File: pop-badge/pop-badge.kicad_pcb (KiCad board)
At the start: 2 copper layers, 155.4 x 107.4 mm, 148 parts, among them J1 Conn_01x04, Q1 BC818, U1 WS2812-2020, U10 WS2812-2020, U11 WS2812-2020, U12 WS2812-2020, U13 WS2812-2020, U14 WS2812-2020, U15 WS2812-2020, U16 WS2812-2020, U17 WS2812-2020, U18 WS2812-2020, U19 WS2812-2020, U2 WS2812-2020, U20 WS2812-2020, U21 WS2812-2020, U22 WS2812-2020, U23 WS2812-2020, U24 WS2812-2020, U25 WS2812-2020, U3 WS2812-2020, U4 WS2812-2020, U5 WS2812-2020, U6 WS2812-2020, U7 WS2812-2020, U8 WS2812-2020, U9 WS2812-2020

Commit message: much more layouting
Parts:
- removed D51, D52, D53, D54, D55, D56, D57, D58, D59, D60: LED, LED_SMD:LED_0603_1608Metric
- removed the R51 at (158.2, 69.0)
- removed R52, R53, R54, R55, R56, R57, R58, R59, R60: 100, Resistor_SMD:R_0603_1608Metric_Pad1.05x0.95mm_HandSolder
- added H1: MountingHole, MountingHole:MountingHole_4.3mm_M4, F.Cu at (48.3, 72.4)
- added H2: MountingHole, MountingHole:MountingHole_4.3mm_M4, F.Cu at (95.2, 72.4)
- J1: moved to B.Cu
- moved R18 122.2 mm to (74.3, 131.6), turned to 270 degrees
- moved R12 109.0 mm to (102.1, 87.2), turned to 90 degrees
- moved R22 107.0 mm to (70.4, 125.1), turned to 270 degrees
- moved R41 106.2 mm to (78.9, 123.8), turned to 270 degrees
- moved R30 102.9 mm to (66.5, 118.0), turned to 270 degrees
- moved R2 102.8 mm to (50.7, 121.7), turned to 270 degrees
- moved D27 102.1 mm to (58.7, 49.4)
- moved R16 100.7 mm to (82.5, 72.8), turned to 90 degrees
- moved R29 98.3 mm to (35.3, 128.9), turned to 180 degrees
- moved R5 97.5 mm to (30.9, 123.7), turned to 180 degrees
- moved R25 95.1 mm to (41.1, 123.3), turned to 270 degrees
- moved R39 94.6 mm to (109.3, 124.5), turned to 270 degrees
- moved R21 91.9 mm to (25.3, 131.1), turned to 180 degrees
- moved R43 90.1 mm to (87.5, 115.2), turned to 270 degrees
- moved D3 88.3 mm to (64.8, 54.0), turned to 180 degrees
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- renumbered R61 to R51
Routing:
- net LEDw+: track 71.9 -> 247.1 mm
- net Net-(U10-Pad1): track 0.00 -> 15.1 mm
- net Net-(U21-Pad1): track 0.00 -> 13.8 mm
- net Net-(U18-Pad1): track 0.00 -> 13.4 mm
- net Net-(U17-Pad1): track 0.00 -> 12.6 mm
- net Net-(U12-Pad1): track 0.00 -> 12.2 mm
- net Net-(U5-Pad1): track 0.00 -> 11.0 mm
- net Net-(U11-Pad1): track 0.00 -> 10.2 mm
- net Net-(U24-Pad1): track 0.00 -> 9.82 mm
- net Net-(U7-Pad1): track 0.00 -> 8.84 mm
- net Net-(U6-Pad1): track 0.00 -> 6.83 mm
- net Net-(U4-Pad1): track 0.00 -> 6.48 mm
- net Net-(U3-Pad1): track 0.00 -> 6.36 mm
- net Net-(U2-Pad1): track 0.00 -> 6.36 mm
- net Net-(U1-Pad1): track 0.00 -> 6.36 mm
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- removed copper zone on B.Cu, net LEDw-
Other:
- board size 155.4 x 107.4 mm -> 129.5 x 101.3 mm

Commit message: routing mostly done
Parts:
- moved R21 3.25 mm to (23.2, 128.5)
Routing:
- net LEDw+: track 247.1 -> 619.3 mm
- net Net-(D20-Pad2): track 0.00 -> 4.20 mm
- net Net-(D14-Pad2): track 0.00 -> 3.43 mm
- net Net-(D12-Pad2): track 0.00 -> 2.95 mm
- net Net-(D36-Pad2): track 0.00 -> 2.95 mm
- net Net-(D23-Pad2): track 0.00 -> 2.88 mm
- net Net-(D31-Pad2): track 0.00 -> 2.82 mm
- net Net-(D27-Pad2): track 0.00 -> 2.82 mm
- net Net-(D3-Pad2): track 0.00 -> 2.82 mm
- net Net-(D42-Pad2): track 0.00 -> 2.78 mm
- net Net-(D11-Pad2): track 0.00 -> 2.72 mm
- net Net-(D47-Pad2): track 0.00 -> 2.69 mm
- net Net-(D33-Pad2): track 0.00 -> 2.66 mm
- net Net-(D38-Pad2): track 0.00 -> 2.53 mm
- net Net-(D45-Pad2): track 0.00 -> 2.52 mm
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
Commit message: current state
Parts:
- moved J1 38.7 mm to (56.9, 108.8), turned to 0 degrees
- moved Q1 33.9 mm to (63.9, 105.7)
- moved R51 32.6 mm to (60.6, 105.0), turned to 180 degrees
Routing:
- net LEDw-: track 3.82 -> 39.8 mm, vias 3 -> 16
- net LEDw+: track 619.3 -> 640.3 mm
- net /RGB LEDs/DIN: track 0.00 -> 14.5 mm, vias 0 -> 2
- net GND: track 0.00 -> 6.39 mm
- added copper zone on B.Cu, net LEDw-

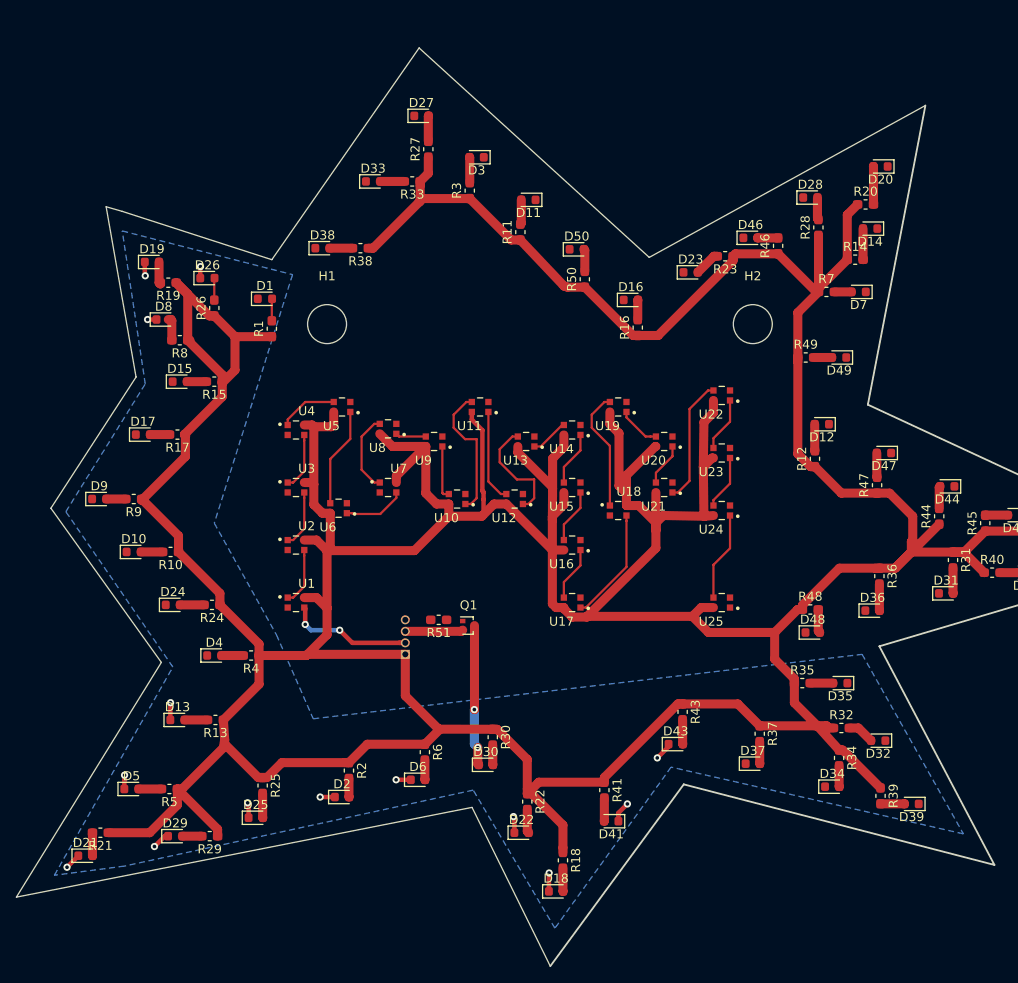
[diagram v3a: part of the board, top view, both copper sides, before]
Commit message: import decoupling caps and remove power lines for redo for ws2812
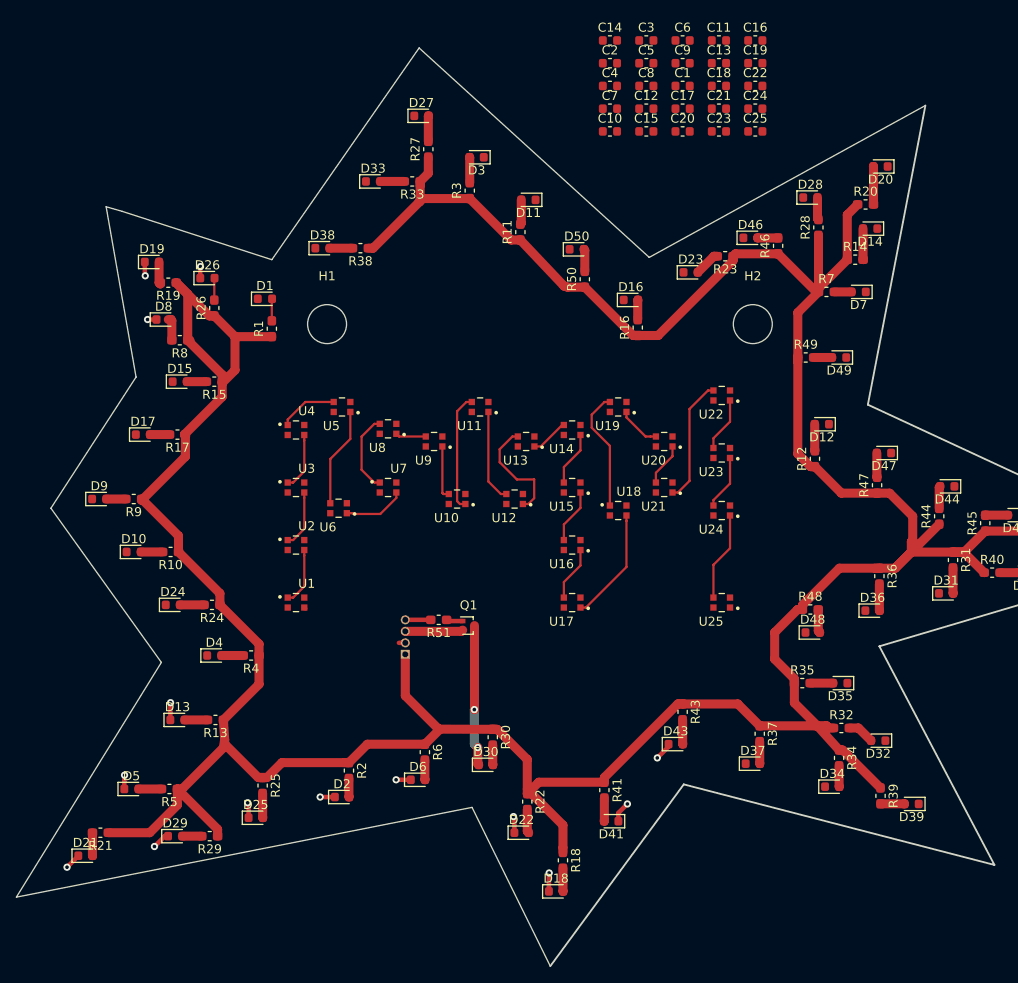
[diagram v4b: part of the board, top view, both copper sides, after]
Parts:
- added C1: 100nF, Capacitor_SMD:C_0603_1608Metric, F.Cu at (87.5, 46.1)
- added C10: 100nF, Capacitor_SMD:C_0603_1608Metric, F.Cu at (79.5, 51.1)
- added C11: 100nF, Capacitor_SMD:C_0603_1608Metric, F.Cu at (91.5, 41.1)
- added C12: 100nF, Capacitor_SMD:C_0603_1608Metric, F.Cu at (83.5, 48.6)
- added C13: 100nF, Capacitor_SMD:C_0603_1608Metric, F.Cu at (91.5, 43.6)
- added C14: 100nF, Capacitor_SMD:C_0603_1608Metric, F.Cu at (79.5, 41.1)
- added C15: 100nF, Capacitor_SMD:C_0603_1608Metric, F.Cu at (83.5, 51.1)
- added C16: 100nF, Capacitor_SMD:C_0603_1608Metric, F.Cu at (95.5, 41.1)
- added C17: 100nF, Capacitor_SMD:C_0603_1608Metric, F.Cu at (87.5, 48.6)
- added C18: 100nF, Capacitor_SMD:C_0603_1608Metric, F.Cu at (91.5, 46.1)
- added C19: 100nF, Capacitor_SMD:C_0603_1608Metric, F.Cu at (95.5, 43.6)
- added C2: 100nF, Capacitor_SMD:C_0603_1608Metric, F.Cu at (79.5, 43.6)
- added C20: 100nF, Capacitor_SMD:C_0603_1608Metric, F.Cu at (87.5, 51.1)
- added C21: 100nF, Capacitor_SMD:C_0603_1608Metric, F.Cu at (91.5, 48.6)
- added C22: 100nF, Capacitor_SMD:C_0603_1608Metric, F.Cu at (95.5, 46.1)
- added C23: 100nF, Capacitor_SMD:C_0603_1608Metric, F.Cu at (91.5, 51.1)
- added C24: 100nF, Capacitor_SMD:C_0603_1608Metric, F.Cu at (95.5, 48.6)
- added C25: 100nF, Capacitor_SMD:C_0603_1608Metric, F.Cu at (95.5, 51.1)
- added C3: 100nF, Capacitor_SMD:C_0603_1608Metric, F.Cu at (83.5, 41.1)
- added C4: 100nF, Capacitor_SMD:C_0603_1608Metric, F.Cu at (79.5, 46.1)
- added C5: 100nF, Capacitor_SMD:C_0603_1608Metric, F.Cu at (83.5, 43.6)
- added C6: 100nF, Capacitor_SMD:C_0603_1608Metric, F.Cu at (87.5, 41.1)
- added C7: 100nF, Capacitor_SMD:C_0603_1608Metric, F.Cu at (79.5, 48.6)
- added C8: 100nF, Capacitor_SMD:C_0603_1608Metric, F.Cu at (83.5, 46.1)
- added C9: 100nF, Capacitor_SMD:C_0603_1608Metric, F.Cu at (87.5, 43.6)
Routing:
- net LEDw+: track 640.3 -> 403.4 mm
- net /RGB LEDs/DIN: track 14.5 -> 0.85 mm, vias 2 -> 0
- net /White LEDs/LEDwMCU: track 0.00 -> 2.81 mm
- net Net-(U10-Pad1): track 15.1 -> 13.0 mm
- net Net-(Q1-Pad1): track 0.00 -> 1.83 mm
- removed copper zone on B.Cu, net LEDw-

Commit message: routing done
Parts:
- added C26: 100u, Capacitor_THT:CP_Radial_D6.3mm_P2.50mm, B.Cu at (49.5, 109.3)
- added R52: 220R, Resistor_SMD:R_0603_1608Metric_Pad1.05x0.95mm_HandSolder, F.Cu at (60.6, 103.6)
- added U26: Pico, RPi_Pico:RPi_Pico_SMD, B.Cu at (72.9, 89.9)
- C1, C10, C11, C12, C13, C14, C15, C16, C17, C18, C19, C2, C20, C21, C22, C23, C24, C25, C3, C4, C5, C6, C7, C8, C9: footprint Capacitor_SMD:C_0603_1608Metric -> Capacitor_SMD:C_0402_1005Metric
- moved C19 65.5 mm to (74.0, 105.5), turned to 90 degrees
- moved C6 64.7 mm to (90.9, 105.7), turned to 90 degrees
- moved C10 60.0 mm to (46.5, 101.2)
- moved C13 58.0 mm to (73.5, 98.7), turned to 180 degrees
- moved C15 57.5 mm to (47.7, 96.1), turned to 180 degrees
- moved C7 55.4 mm to (46.8, 93.3)
- moved C12 54.6 mm to (47.7, 89.9), turned to 180 degrees
- moved C3 53.9 mm to (53.6, 86.0)
- moved C14 53.1 mm to (55.4, 88.5)
- moved C5 52.4 mm to (49.4, 83.4), turned to 180 degrees
- moved C1 51.9 mm to (68.0, 94.2), turned to 90 degrees
- moved C11 51.9 mm to (85.0, 92.5), turned to 180 degrees
- moved C16 51.7 mm to (81.2, 90.8)
- moved C8 51.6 mm to (47.4, 83.0), turned to 270 degrees
- moved C9 50.7 mm to (73.6, 92.4), turned to 180 degrees
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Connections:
- net /White LEDs/LEDwMCU renamed LEDwMCU
- net LEDw+ renamed +5V
- J1 pad 2: /RGB LEDs/DIN -> DIN
- U1 pad 3: /RGB LEDs/DIN -> Net-(R52-Pad1)
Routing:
- net +5V: track 403.4 -> 824.7 mm, vias 0 -> 1
- net GND: track 6.39 -> 225.4 mm, vias 0 -> 24
- net LEDw-: track 39.8 -> 9.72 mm, vias 16 -> 2
- net LEDwMCU: track 2.81 -> 19.1 mm, vias 0 -> 2
- net DIN: track 0.00 -> 15.4 mm, vias 0 -> 1
- net Net-(R52-Pad1): track 0.00 -> 14.1 mm, vias 0 -> 2
- net Net-(Q1-Pad1): track 1.83 -> 3.10 mm
- net /RGB LEDs/DIN: track 0.85 -> 0.00 mm
- net Net-(D48-Pad2): track 2.61 -> 1.80 mm
- added copper zone on B.Cu, net GND
- added copper zone on F.Cu, net LEDw-

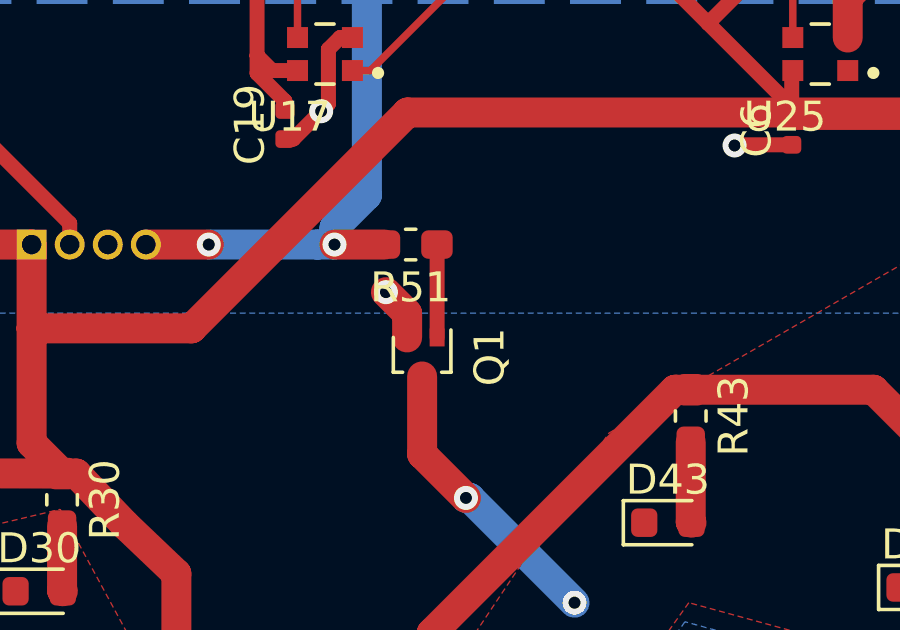
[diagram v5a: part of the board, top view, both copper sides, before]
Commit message: different BJT again
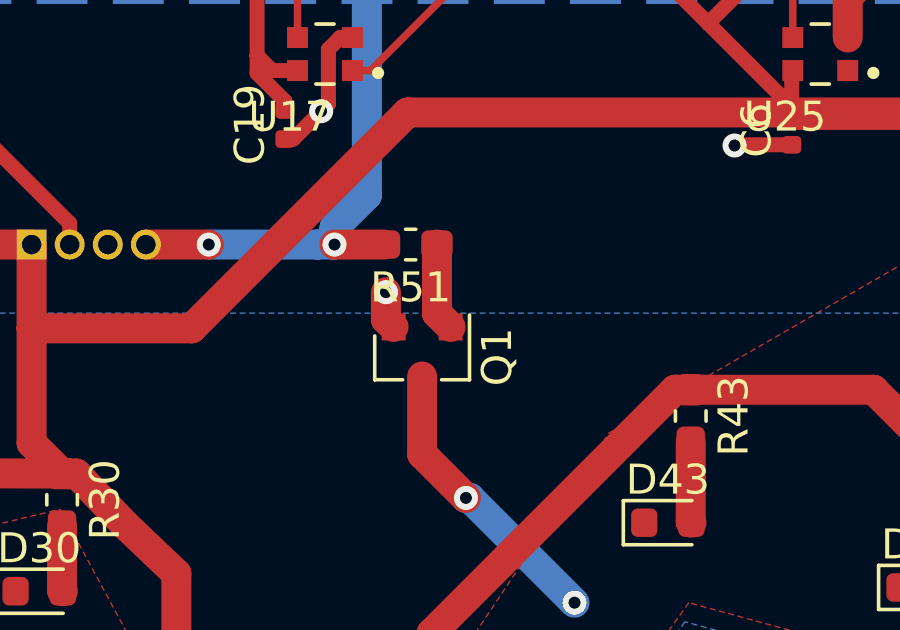
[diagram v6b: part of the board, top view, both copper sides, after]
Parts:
- Q1: footprint Package_TO_SOT_SMD:SOT-416 -> Package_TO_SOT_SMD:SOT-23
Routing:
- net GND: track 225.4 -> 224.9 mm
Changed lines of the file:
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@@
     (thickness 1.6)
     (drawings 17)
-    (tracks 729)
+    (tracks 730)
     (zones 0)
     (modules 158)
@@
     (add_net "Net-(U8-Pad1)")
   )
-  (module Package_TO_SOT_SMD:SOT-416 (layer F.Cu)
+  (module Package_TO_SOT_SMD:SOT-23 (layer F.Cu)
     (at 78.5495 113.2205 270)
-    (descr "SOT-416, https://www.nxp.com/docs/en/package-information/SOT416.pdf")
-    (tags SOT-416)
+    (descr "SOT-23, Standard")
+    (tags SOT-23)
     (attr smd)
-    (fp_text reference Q1 (at 0 -2.25 90) (layer F.SilkS)
+    (fp_text reference Q1 (at 0 -2.5 90) (layer F.SilkS)
       (effects (font (size 1 1) (thickness 0.15)))
     )
-    (fp_text value BC818 (at 0 2.25 90) (layer F.Fab)
+    (fp_text value BC818 (at 0 2.5 90) (layer F.Fab)
       (effects (font (size 1 1) (thickness 0.15)))
     )
-    (fp_line (start -0.15 -0.9) (end -0.45 -0.6) (layer F.Fab) (width 0.1))
-    (fp_line (start 0.51 0.96) (end -0.65 0.96) (layer F.SilkS) (width 0.12))
-    (fp_line (start 0.51 -0.96) (end -0.9 -0.96) (layer F.SilkS) (width 0.12))
-    (fp_line (start -1.2 1.15) (end -1.2 -1.15) (layer F.CrtYd) (width 0.05))
-    (fp_line (start 1.2 1.15) (end -1.2 1.15) (layer F.CrtYd) (width 0.05))
-    (fp_line (start 1.2 -1.15) (end 1.2 1.15) (layer F.CrtYd) (width 0.05))
-    (fp_line (start -1.2 -1.15) (end 1.2 -1.15) (layer F.CrtYd) (width 0.05))
-    (fp_line (start 0.51 -0.96) (end 0.51 -0.65) (layer F.SilkS) (width 0.12))
-    (fp_line (start 0.51 0.96) (end 0.51 0.65) (layer F.SilkS) (width 0.12))
-    (fp_line (start -0.45 0.9) (end 0.45 0.9) (layer F.Fab) (width 0.1))
-    (fp_line (start 0.45 -0.9) (end 0.45 0.9) (layer F.Fab) (width 0.1))
-    (fp_line (start -0.15 -0.9) (end 0.45 -0.9) (layer F.Fab) (width 0.1))
-    (fp_line (start -0.45 -0.6) (end -0.45 0.9) (layer F.Fab) (width 0.1))
+    (fp_line (start 0.76 1.58) (end -0.7 1.58) (layer F.SilkS) (width 0.12))
+    (fp_line (start 0.76 -1.58) (end -1.4 -1.58) (layer F.SilkS) (width 0.12))
+    (fp_line (start -1.7 1.75) (end -1.7 -1.75) (layer F.CrtYd) (width 0.05))
+    (fp_line (start 1.7 1.75) (end -1.7 1.75) (layer F.CrtYd) (width 0.05))
+    (fp_line (start 1.7 -1.75) (end 1.7 1.75) (layer F.CrtYd) (width 0.05))
+    (fp_line (start -1.7 -1.75) (end 1.7 -1.75) (layer F.CrtYd) (width 0.05))
+    (fp_line (start 0.76 -1.58) (end 0.76 -0.65) (layer F.SilkS) (width 0.12))
+    (fp_line (start 0.76 1.58) (end 0.76 0.65) (layer F.SilkS) (width 0.12))
+    (fp_line (start -0.7 1.52) (end 0.7 1.52) (layer F.Fab) (width 0.1))
+    (fp_line (start 0.7 -1.52) (end 0.7 1.52) (layer F.Fab) (width 0.1))
+    (fp_line (start -0.7 -0.95) (end -0.15 -1.52) (layer F.Fab) (width 0.1))
+    (fp_line (start -0.15 -1.52) (end 0.7 -1.52) (layer F.Fab) (width 0.1))
+    (fp_line (start -0.7 -0.95) (end -0.7 1.5) (layer F.Fab) (width 0.1))
     (fp_text user %R (at 0 0) (layer F.Fab)
-      (effects (font (size 0.35 0.35) (thickness 0.05)))
+      (effects (font (size 0.5 0.5) (thickness 0.075)))
     )
-    (pad 3 smd rect (at 0.65 0 270) (size 0.6 0.5) (layers F.Cu F.Paste F.Mask)
+    (pad 3 smd rect (at 1 0 270) (size 0.9 0.8) (layers F.Cu F.Paste F.Mask)
       (net 2 LEDw-))
-    (pad 2 smd rect (at -0.65 0.5 270) (size 0.6 0.5) (layers F.Cu F.Paste F.Mask)
+    (pad 2 smd rect (at -1 0.95 270) (size 0.9 0.8) (layers F.Cu F.Paste F.Mask)
       (net 32 GND))
-    (pad 1 smd rect (at -0.65 -0.5 270) (size 0.6 0.5) (layers F.Cu F.Paste F.Mask)
+    (pad 1 smd rect (at -1 -0.95 270) (size 0.9 0.8) (layers F.Cu F.Paste F.Mask)
       (net 34 "Net-(Q1-Pad1)"))
-    (model ${KISYS3DMOD}/Package_TO_SOT_SMD.3dshapes/SOT-416.wrl
+    (model ${KISYS3DMOD}/Package_TO_SOT_SMD.3dshapes/SOT-23.wrl
       (at (xyz 0 0 0))
       (scale (xyz 1 1 1))
@@
   (segment (start 65.655998 80.984) (end 65.1915 81.448498) (width 0.5) (layer F.Cu) (net 32))
   (segment (start 66.066 80.984) (end 65.655998 80.984) (width 0.5) (layer F.Cu) (net 32))
-  (segment (start 78.0495 111.768) (end 77.343 111.0615) (width 1) (layer F.Cu) (net 32))
   (via (at 77.343 111.0615) (size 0.8) (drill 0.4) (layers F.Cu B.Cu) (net 32))
-  (segment (start 78.0495 112.5705) (end 78.0495 111.768) (width 1) (layer F.Cu) (net 32))
+  (segment (start 77.343 111.964) (end 77.5995 112.2205) (width 1) (layer F.Cu) (net 32))
+  (segment (start 77.343 111.0615) (end 77.343 111.964) (width 1) (layer F.Cu) (net 32))
   (segment (start 61.667106 103.632) (end 61.454 103.632) (width 0.5) (layer F.Cu) (net 33))
   (segment (start 66.802 109.474) (end 66.802 108.766894) (width 0.5) (layer F.Cu) (net 33))
@@
   (segment (start 64.008 98.806) (end 64.008 105.845894) (width 0.5) (layer B.Cu) (net 33))
   (segment (start 79.0495 109.48) (end 79.0435 109.474) (width 0.5) (layer F.Cu) (net 34))
-  (segment (start 79.0495 112.5705) (end 79.0495 109.48) (width 0.5) (layer F.Cu) (net 34))
+  (segment (start 79.0435 111.7645) (end 79.4995 112.2205) (width 1) (layer F.Cu) (net 34))
+  (segment (start 79.0435 109.474) (end 79.0435 111.7645) (width 1) (layer F.Cu) (net 34))
   (segment (start 43.916 98.554) (end 43.916 102.574) (width 0.25) (layer F.Cu) (net 35))
   (segment (start 45.146 97.324) (end 43.916 98.554) (width 0.25) (layer F.Cu) (net 35))
